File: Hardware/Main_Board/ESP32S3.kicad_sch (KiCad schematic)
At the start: 1 part, among them U1 ESP32-S3-DEVKITC-1U-N8R2

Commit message: added 2 more sheets
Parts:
- added DWM1: DWM1000, RF_Module:DWM1000, symbol RF_Module:DWM1000
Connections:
- net 3V3: now also DWM1.5 (VDDAON), DWM1.6 (VDD3V3), DWM1.7 (VDD3V3)
- net GND: now also DWM1.16 (VSS), DWM1.21 (VSS), DWM1.23 (VSS), DWM1.24 (VSS), DWM1.8 (VSS)
- new net ESP_CLK: DWM1.20 (SPICLK)
- new net ESP_CS: DWM1.17 (~{SPICS})
- new net ESP_MISO: DWM1.19 (SPIMISO)
- new net ESP_MOSI: DWM1.18 (SPIMOSI)
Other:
- note added: "DWM1000 UWB Module"
- note removed: "Decoupling Capacitors"

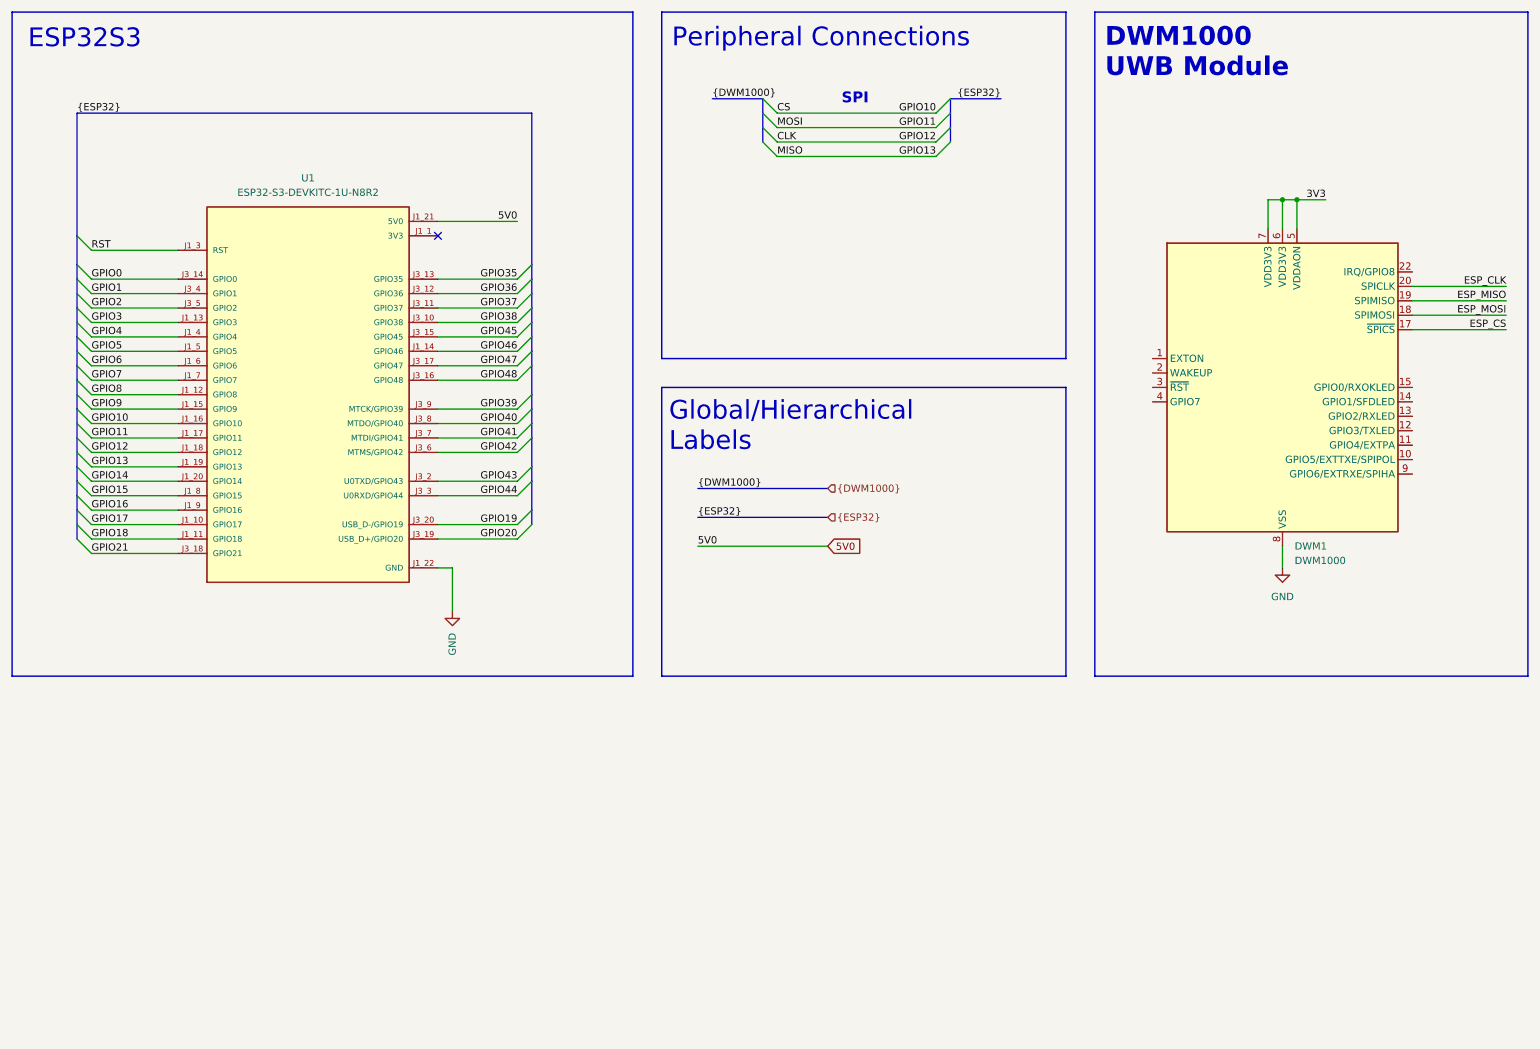
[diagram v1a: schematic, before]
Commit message: Mixed in all of Layth's work, and added extra sheets
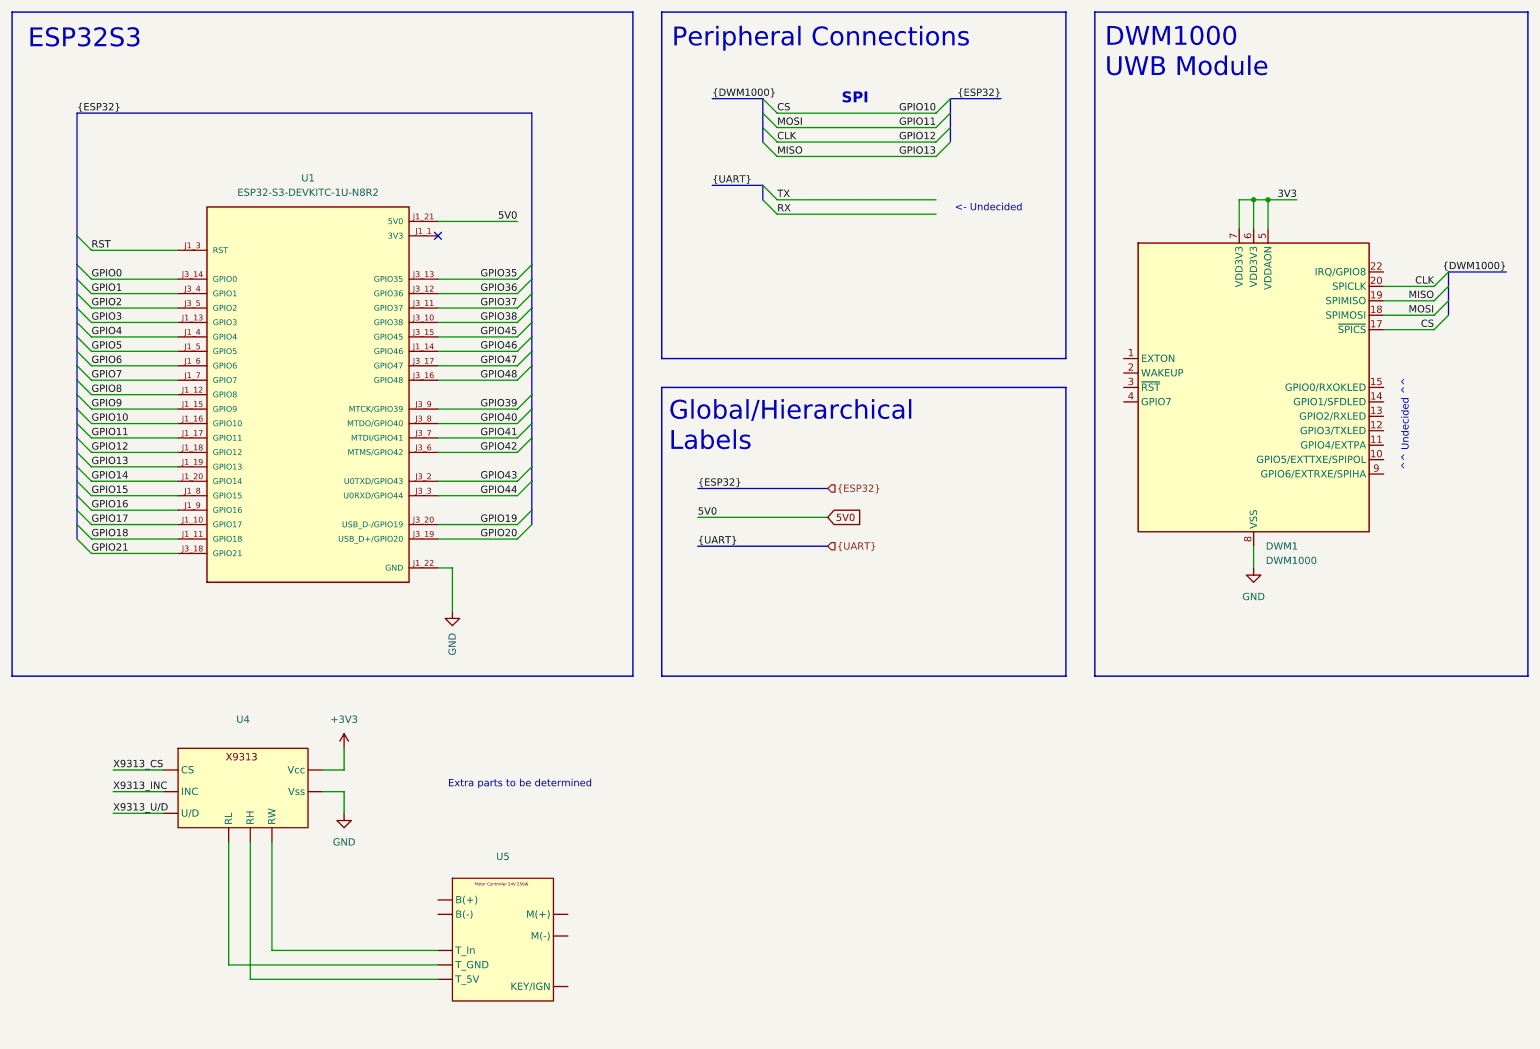
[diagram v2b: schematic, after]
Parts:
- added U4: ~, symbol ESP32-Symbols:X9313
- added U5: ~, symbol ESP32-Symbols:MotoController
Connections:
- net ESP_CLK is gone; now on net CLK: DWM1.20 (SPICLK)
- net ESP_CS is gone; now on net CS: DWM1.17 (~{SPICS})
- net ESP_MISO is gone; now on net GPIO13: DWM1.19 (SPIMISO)
- net ESP_MOSI is gone; now on net GPIO11: DWM1.18 (SPIMOSI)
- net GND: now also U4. (Vss)
- new net: U4. (Vss), U5. (KEY/IGN) (x3)
- new net +3V3: U4. (Vss)
- new net X9313_CS: U4. (Vss)
- new net X9313_INC: U4. (Vss)
- new net X9313_U/D: U4. (Vss)
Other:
- note added: "<- Undecided"
- note added: "Extra parts to be determined"
- note added: "^^ Undecided ^^"
- moved on the sheet: DWM1
